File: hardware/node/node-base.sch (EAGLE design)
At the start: 56 parts, among them IC1 HYPERTRIANGLE_TCS3472FN, Q1 32.768kHz, Q2 24MHz, Q3 BS250, U1 INA322_DGK_8, U2 LMV551_DBV_5, X1 BU-SMA-V

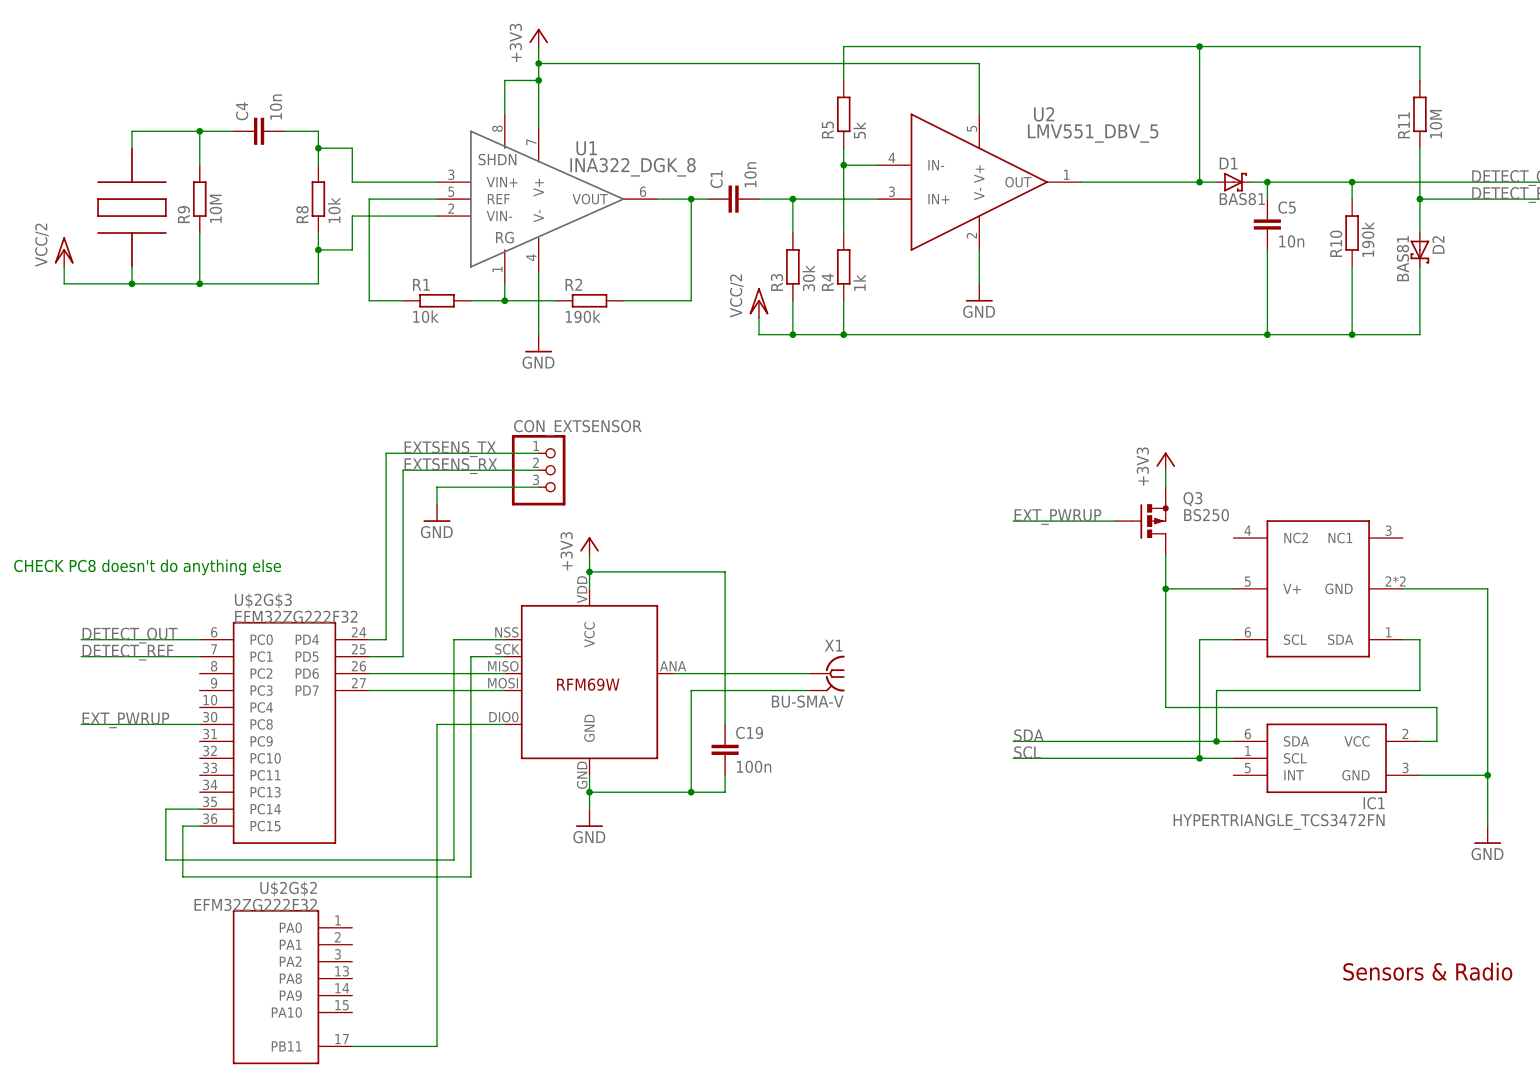
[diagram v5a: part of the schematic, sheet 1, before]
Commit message: NODEHW: Some components placed...
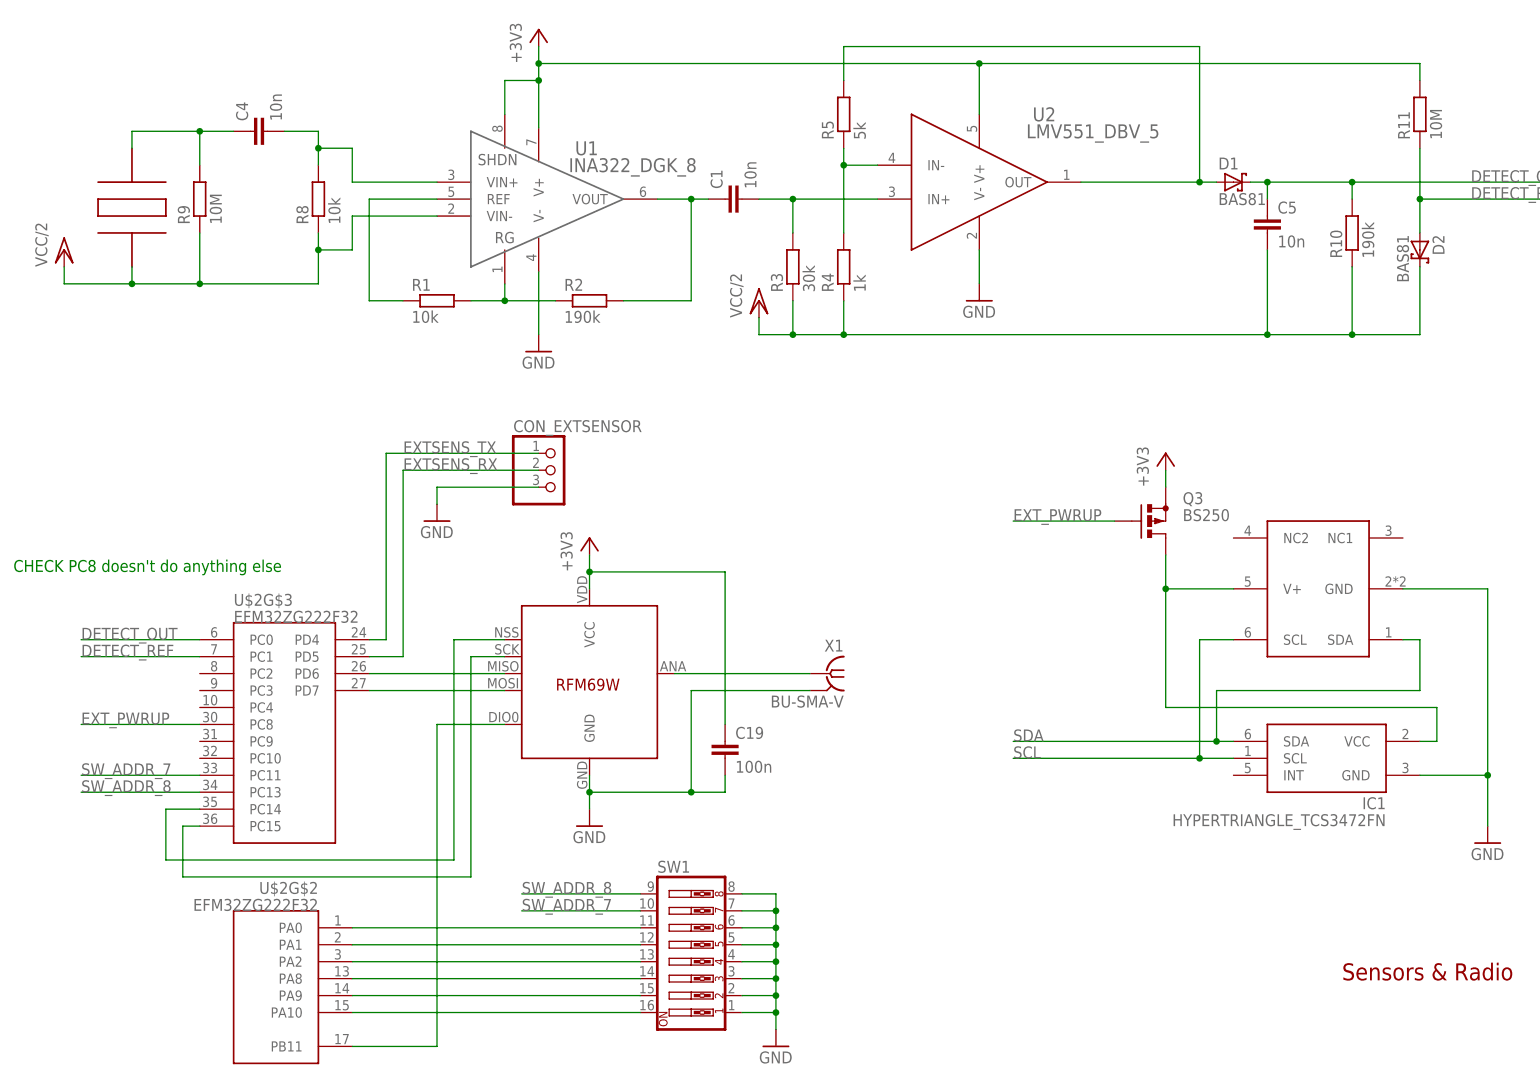
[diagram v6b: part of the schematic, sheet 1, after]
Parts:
- added SW1: (no value), SparkFun-Electromechanical:SW_DIP-8
- D1, D2: device diode:SCHOTTKY-DIODECB417-15 -> diode:SCHOTTKY-DIODEDO35-7
- R6, R7: device resistor:R-EU_0309/12 -> resistor:R-EU_0204/7
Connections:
- new net SW_ADDR_1: SW1.16, U$2G$2.PA10
- new net SW_ADDR_2: SW1.15, U$2G$2.PA9
- new net SW_ADDR_3: SW1.14, U$2G$2.PA8
- new net SW_ADDR_4: SW1.13, U$2G$2.PA2
- new net SW_ADDR_5: SW1.12, U$2G$2.PA1
- new net SW_ADDR_6: SW1.11, U$2G$2.PA0
- new net SW_ADDR_7: SW1.10, U$2G$3.PC11
- new net SW_ADDR_8: SW1.9, U$2G$3.PC13
- net +3V3: now also R11.2
- net GND: now also SW1.1, SW1.2, SW1.3, SW1.4, SW1.5, SW1.6, SW1.7, SW1.8
- net OPAMP_OUT: no longer R11.2

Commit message: NODEHW: Routeing starts
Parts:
- C14, C15, C6, C7, C8, C9: device SparkFun-Capacitors:CAPPTH -> SparkFun-Capacitors:CAP0805
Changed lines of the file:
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@@
 <part name="+3V3" library="supply1" deviceset="+3V3" device=""/>
 <part name="GND4" library="supply1" deviceset="GND" device=""/>
-<part name="C6" library="SparkFun-Capacitors" deviceset="CAP" device="PTH" value="100n"/>
-<part name="C7" library="SparkFun-Capacitors" deviceset="CAP" device="PTH" value="100n"/>
-<part name="C8" library="SparkFun-Capacitors" deviceset="CAP" device="PTH" value="100n"/>
-<part name="C9" library="SparkFun-Capacitors" deviceset="CAP" device="PTH" value="100n"/>
+<part name="C6" library="SparkFun-Capacitors" deviceset="CAP" device="0805" value="100n"/>
+<part name="C7" library="SparkFun-Capacitors" deviceset="CAP" device="0805" value="100n"/>
+<part name="C8" library="SparkFun-Capacitors" deviceset="CAP" device="0805" value="100n"/>
+<part name="C9" library="SparkFun-Capacitors" deviceset="CAP" device="0805" value="100n"/>
 <part name="C10" library="SparkFun-Capacitors" deviceset="CAP_POL" device="PTH2" value="10u"/>
 <part name="+3V4" library="supply1" deviceset="+3V3" device=""/>
@@
 <part name="GND7" library="supply1" deviceset="GND" device=""/>
 <part name="GND8" library="supply1" deviceset="GND" device=""/>
-<part name="C14" library="SparkFun-Capacitors" deviceset="CAP" device="PTH" value="7p5"/>
-<part name="C15" library="SparkFun-Capacitors" deviceset="CAP" device="PTH" value="7p5"/>
+<part name="C14" library="SparkFun-Capacitors" deviceset="CAP" device="0805" value="7p5"/>
+<part name="C15" library="SparkFun-Capacitors" deviceset="CAP" device="0805" value="7p5"/>
 <part name="C16" library="SparkFun-Capacitors" deviceset="CAP" device="PTH" value="7p5"/>
 <part name="C17" library="SparkFun-Capacitors" deviceset="CAP" device="PTH" value="7p5"/>

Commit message: NODEHW: Routeing ongoing
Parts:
- CON_EXTSENSOR: device pinhead:PINHD-1X3 -> pinhead:PINHD-1X4
- renumbered JP1 to DEBUG
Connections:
- net +3V3: now also CON_EXTSENSOR.1
- net EXTSENS_RX: now also CON_EXTSENSOR.3; no longer CON_EXTSENSOR.2
- net EXTSENS_TX: now also CON_EXTSENSOR.2; no longer CON_EXTSENSOR.1
- net GND: now also CON_EXTSENSOR.4; no longer CON_EXTSENSOR.3
